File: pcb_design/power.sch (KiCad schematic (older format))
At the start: 38 parts, among them Q1 BSC340N08, Q3 AO4805, U11 LM3488, U13 LM1117IMP-v.v, U9 LM22676QTJ-5.0

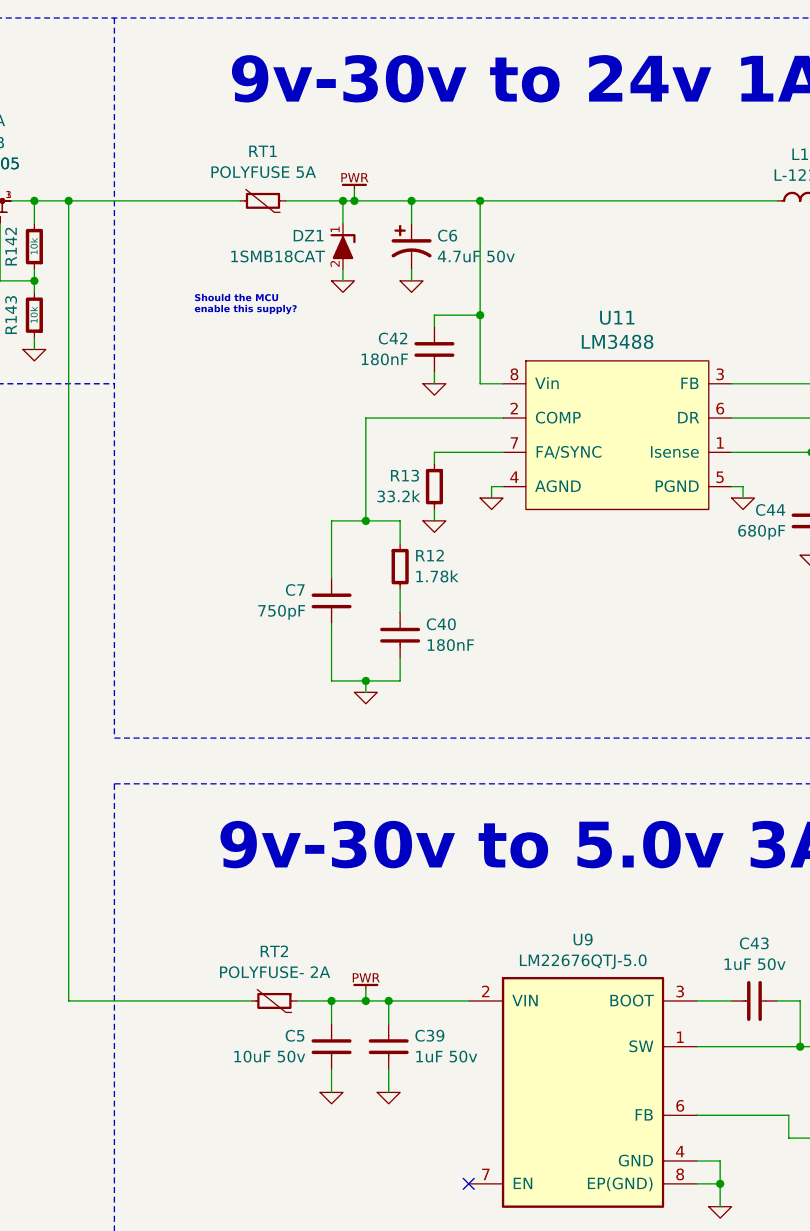
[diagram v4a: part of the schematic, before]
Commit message: Completed some part numbers
Signed-off-by: Marcos Chaparro <mchaparro@paltatech.com>
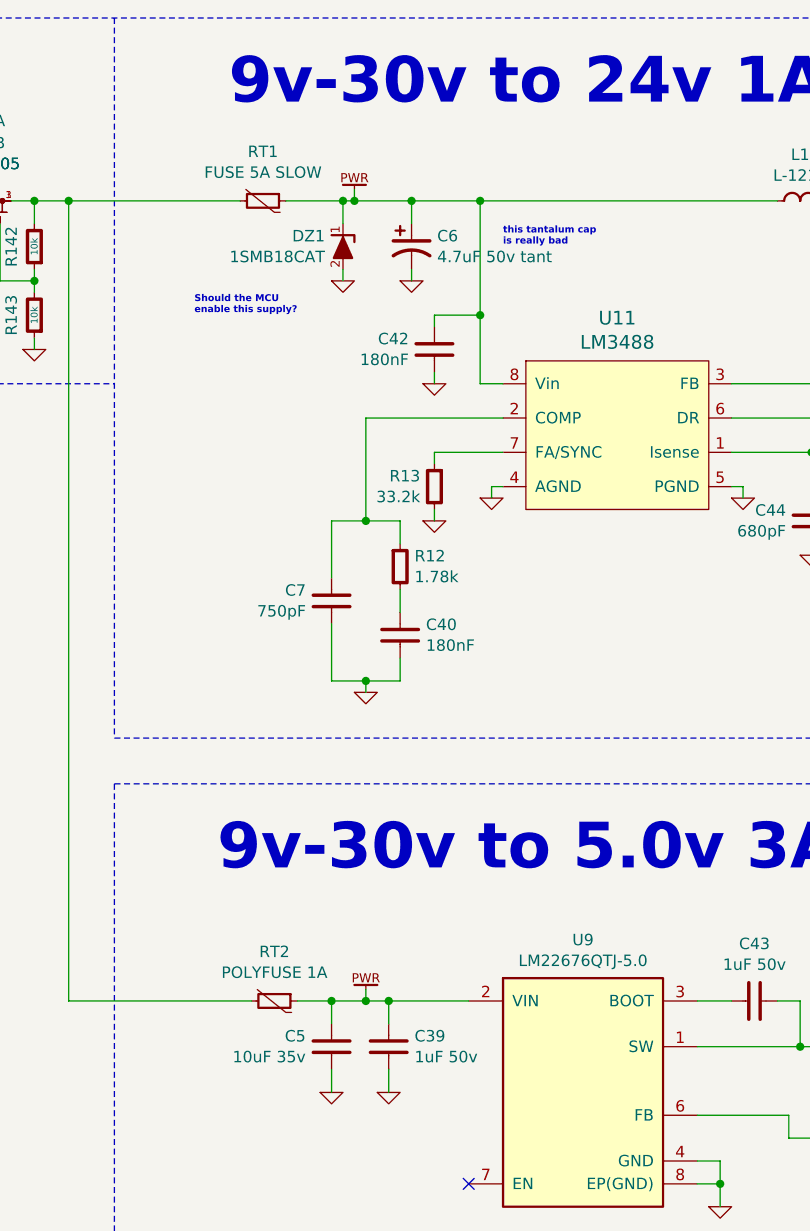
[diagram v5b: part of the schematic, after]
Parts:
- C39, C43: MFR (none) -> Taiyo Yuden; MPN (none) -> UMK212B7105KG-T; SPN (none) -> UMK212B7105KG-T; SPR (none) -> Digikey
- C40: BOM CAP MLCC 100pF C0G 50V 5% [0603] -> CAP MLCC 180nF X7R 50V 5% [0603]; MFR (none) -> Murata Electronics North America; MPN (none) -> GRM188R71E184KA88D; SPN (none) -> 490-6431-1-ND; SPR (none) -> Digikey
- C42: MFR (none) -> Murata Electronics North America; MPN (none) -> GRM188R71E184KA88D; SPN (none) -> 490-6431-1-ND; SPR (none) -> Digikey
- C44, C7: MFR (none) -> Samsung Electro-Mechanics America, Inc.; MPN (none) -> CL21C751JBCNNNC; SPN (none) -> 1276-2691-1-ND; SPR (none) -> Digikey
- C45: MFR (none) -> Murata Electronics North America; MPN (none) -> GRM31CR71H225KA88L; SPN (none) -> 490-3367-1-ND; SPR (none) -> Digikey
- C46, C47, C49, C52: MFR (none) -> Taiyo Yuden; MPN (none) -> LMK316AB7226ML-TR; SPN (none) -> 587-2782-1-ND; SPR (none) -> Digikey
- C48, C50: MFR (none) -> TDK Corporation; MPN (none) -> C2012X5R1V226M125AC; SPN (none) -> 445-14428-1-ND; SPR (none) -> Digikey
- C5: value 10uF 50v -> 10uF 35v; BOM CAP MLCC 100pF C0G 50V 5% [1206] -> CAP MLCC 10uF X7R 35V 5% [1206]; MFR (none) -> Taiyo Yuden; MPN (none) -> GMK316AB7106KL-TR; SPN (none) -> 587-3007-1-ND; SPR (none) -> Digikey
- C51: MFR (none) -> Murata Electronics North America; MPN (none) -> GRM188R71E104KA01D; SPN (none) -> 490-1524-1-ND; SPR (none) -> Digikey
- C6: value 4.7uF 50v -> 4.7uF 50v tant; BOM CAP TANT 0µF 25V 10% [7343] -> CAP TANT 4.7µF 50V 10% [7343]; MFR (none) -> Vishay Sprague; MPN (none) -> 593D475X9050D2TE3; SPN (none) -> 718-1107-1-ND; SPR (none) -> Digikey
- Q1: MFR (none) -> Infineon Technologies; MPN (none) -> BSC340N08NS3GATMA1; SPN (none) -> BSC340N08NS3GATMA1CT-ND; SPR (none) -> Digikey
- R37: MFR (none) -> Susumu; MPN (none) -> PRL1632-R018-F-T1; SPN (none) -> PRL1632.018FCT-ND; SPR (none) -> Digikey
- RT1: value POLYFUSE 5A -> FUSE 5A SLOW; MFR (none) -> Bel Fuse Inc.; MPN (none) -> C1S 5; SPN (none) -> 507-1194-1-ND; SPR (none) -> Digikey
- RT2: value POLYFUSE- 2A -> POLYFUSE 1A; MFR (none) -> Bel Fuse Inc.; MPN (none) -> 0ZCJ0050AF2E; SPN (none) -> 507-1803-1-ND; SPR (none) -> Digikey
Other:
- note added: "this tantalum cap\nis really bad"

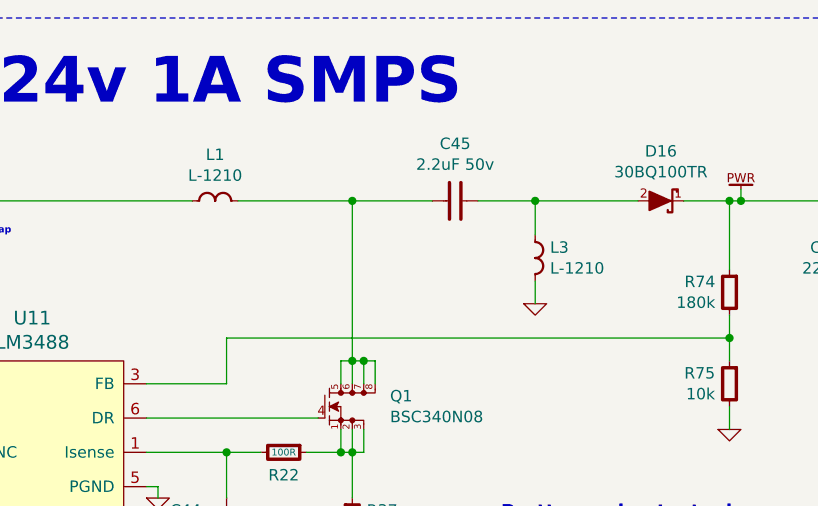
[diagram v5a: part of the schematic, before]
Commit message: Completed part number, manufacturer, etc fields. Simulated analog conditioning
Signed-off-by: Marcos Chaparro <mchaparro@paltatech.com>
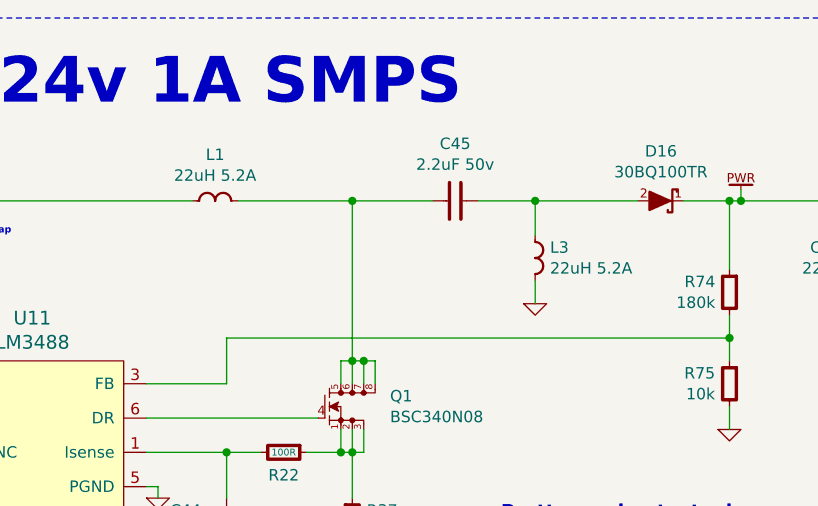
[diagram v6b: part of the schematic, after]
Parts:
- D15, D17: MFR (none) -> Fairchild/ON Semiconductor; MPN (none) -> SS16; SPN (none) -> SS16FSCT-ND; SPR (none) -> Digikey
- D16: MFR (none) -> SMC Diode Solutions; MPN (none) -> 30BQ100TR; SPN (none) -> 1655-1389-1-ND; SPR (none) -> Digikey
- DZ1: MFR (none) -> ON Semiconductor; MPN (none) -> 1SMB18CAT3G; SPN (none) -> 1SMB18CAT3GOSCT-ND; SPR (none) -> Digikey
- L1, L3: value L-1210 -> 22uH 5.2A; MFR (none) -> Bourns Inc.; MPN (none) -> SRR1210-220M; SPN (none) -> SRR1210-220MCT-ND; SPR (none) -> Digikey
- L2: MFR (none) -> Bourns Inc.; MPN (none) -> SDR1307-270ML; SPN (none) -> SDR1307-270MLCT-ND; SPR (none) -> Digikey
- Q3: MFR (none) -> Alpha & Omega Semiconductor Inc.; MPN (none) -> AO4805; SPN (none) -> 785-1055-1-ND; SPR (none) -> Digikey
- R12: MFR (none) -> Yageo; MPN (none) -> RC0603FR-071K78L; SPN (none) -> 311-1.78KHRCT-ND; SPR (none) -> Digikey
- R13: MFR (none) -> Yageo; MPN (none) -> RC0603FR-0733K2L; SPN (none) -> 311-33.2KHRCT-ND; SPR (none) -> Digikey
- R142, R143, R75: MFR (none) -> Yageo; MPN (none) -> RC0603FR-0710KL; SPN (none) -> 311-10.0KHRCT-ND; SPR (none) -> Digikey
- R22: MFR (none) -> Yageo; MPN (none) -> RC0603FR-07100RL; SPN (none) -> 311-100HRCT-ND; SPR (none) -> Digikey
- R74: MFR (none) -> Yageo; MPN (none) -> RC0603FR-07180KL; SPN (none) -> 311-180KHRCT-ND; SPR (none) -> Digikey
- U11: MFR (none) -> Texas Instruments; MPN (none) -> LM3488MM/NOPB; SPN (none) -> LM3488MM/NOPBCT-ND; SPR (none) -> Digikey
- U13: MFR (none) -> Texas Instruments; MPN (none) -> LM1117IMP-3.3/NOPB; SPN (none) -> LM1117IMP-3.3/NOPBCT-ND; SPR (none) -> Digikey
- U9: MFR (none) -> Texas Instruments; MPN (none) -> LM22676QTJE-5.0/NOPB; SPN (none) -> LM22676QTJE-5.0/NOPBCT-ND; SPR (none) -> Digikey

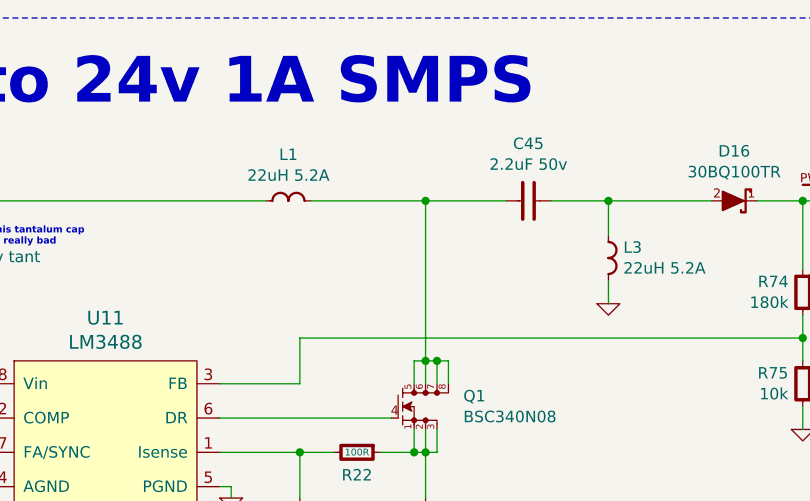
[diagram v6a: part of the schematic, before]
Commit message: Corrected phase current gain. More 3d models
Signed-off-by: Marcos Chaparro <mchaparro@paltatech.com>
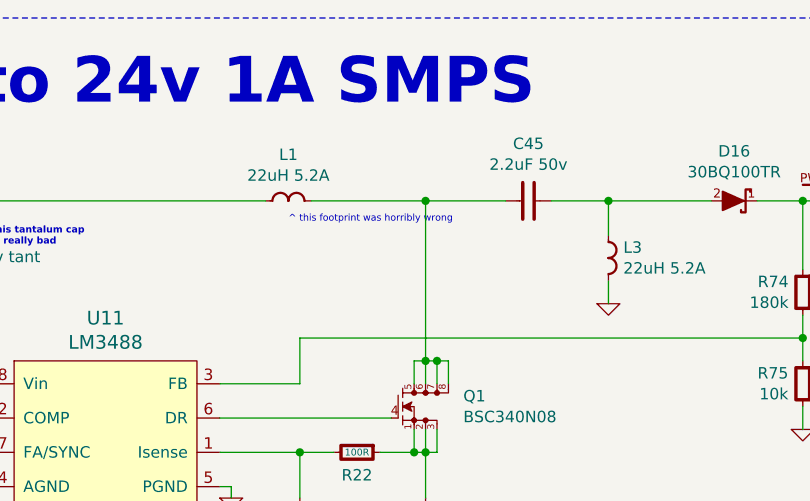
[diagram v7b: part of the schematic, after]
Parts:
- L1, L3: footprint IPC7351-Nominal:INDC3225X135 -> manuf:BOURNS-SRR1210
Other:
- note added: "^ this footprint was horribly wrong"

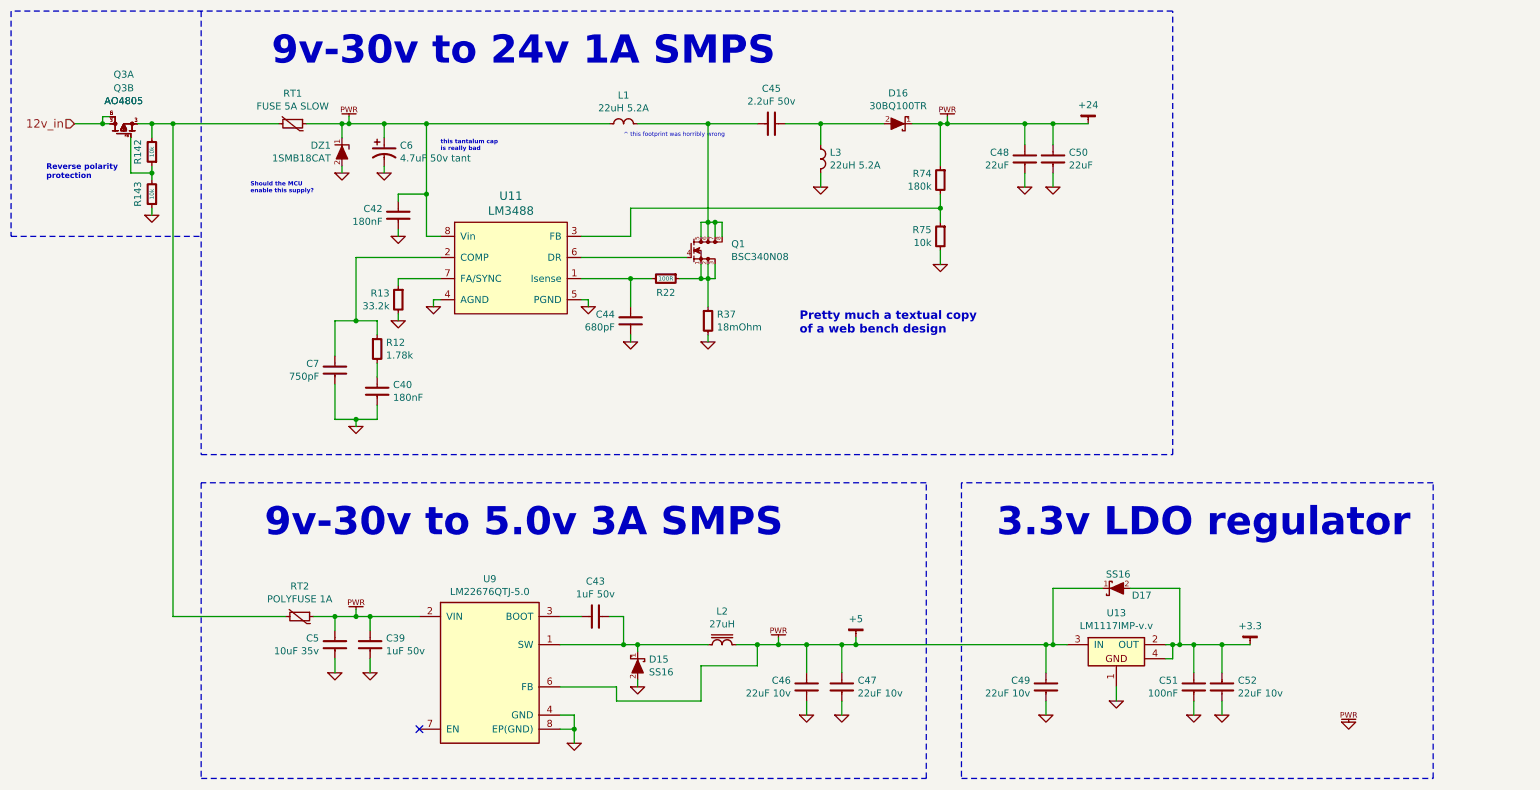
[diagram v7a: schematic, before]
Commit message: Added individual temperature sensing for each half bridge and 2 pwm gpio with low side driver
Signed-off-by: Marcos Chaparro <mchaparro@paltatech.com>
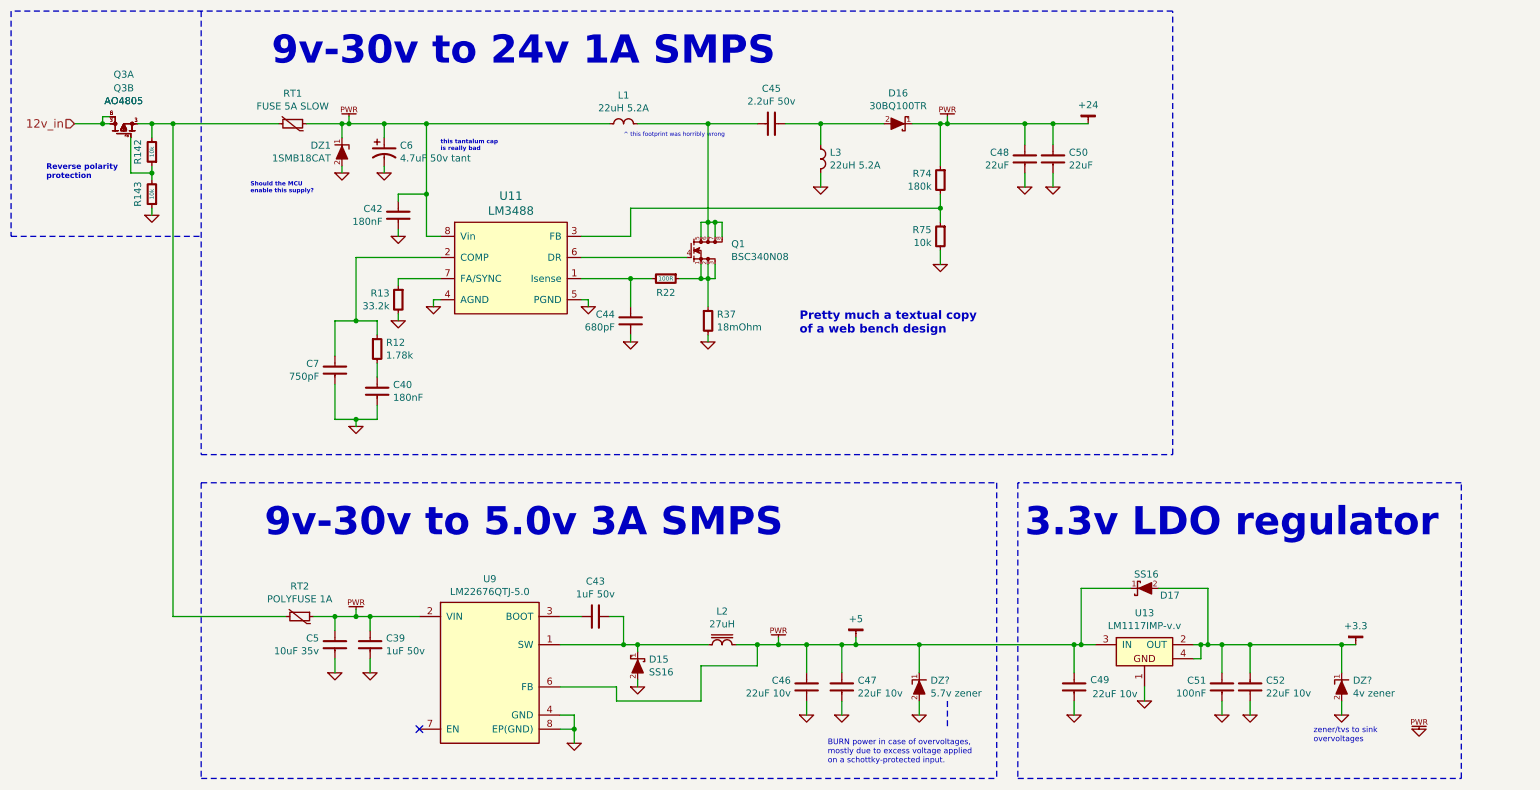
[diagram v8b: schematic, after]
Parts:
- added DZ?: 4v zener, IPC7351-Nominal:DIOM5226X203, symbol 1SMA59xxBT3G
- added DZ?: 5.7v zener, IPC7351-Nominal:DIOM5226X203, symbol 1SMA59xxBT3G
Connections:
- net +3.3: now also DZ?.1 (K)
- net +5: now also DZ?.1 (K)
- net GND: now also DZ?.2 (A), DZ?.2 (A)
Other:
- note added: "BURN power in case of overvoltages,\nmostly due to excess voltage applied\non a schottky-protected input."
- note added: "zener/tvs to sink\novervoltages"
- moved on the sheet: C49, C51, C52, D17, U13
